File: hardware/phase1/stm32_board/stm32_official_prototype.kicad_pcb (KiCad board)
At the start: 6 copper layers, 75 parts, among them CN11 Conn_02x36_Odd_Even, CN12 Conn_02x36_Odd_Even, CN14 USB_B_Micro, CN5 Conn_ARM_JTAG_SWD_10, U1 STM32L496ZGTx, U12 STMPS2151STR, U4 ST890CDR, U5 USBLC6-2SC6, U6 LD39050PU33R, U8 TSV631AILT

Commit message: stm32 board update (1.11.25)
- correcting footprints (IP)
- left off on USB circuitry
- note: net labels must be corrected for differential pair
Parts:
- removed C11, C20, C26: 100nF, Capacitor,100nF,10%,16V,X7R,0603,YAGEO:CC0603N_YAG
- removed C16, C42: 4.7uF, TAN Capacitor,4.7uF,10%,16V,A Type,AVX:TAJA_AVX
- removed C17: 10uF, TAN Capacitor,10uF,10%,16V,A Type,AVX:CAPMP3216X180N
- removed C18: 10uF(25V), Tan Capacitor,10uF,10%,25V,Tan-B,TAJB106K025RNJ:CAPMP3516X190N
- removed C19, C27: 1uF_X5R_0603, Capacitor,1uF,0603,16V,10%,X5R,YAGEO:CAPC1608X90
- removed C45: 100nF, HDR_1x2_2R54:61300211121
- removed JP5: Conn_02x01, HDR_1x2_2R54:61300211121
- removed JP6: Conn_02x04_Odd_Even, 2x4_2R54:61300821121
- removed LD5, LD7: Red, LED-SMD-RED-DIFFUSED_0603_:LED-0603
- removed LD6, LD8: Green, SMD-LED-CLEAR-GREEN_0603_:LED-0603
- removed R22, R28: 1K, RC0603FR-071KL:RESC1607X60N
- removed R26, R52: 10K, RC0603FR-0710KL:RESC1607X60N
- removed R27: 2K7, RES_2.7K_0603_:R0603
- removed R41: 330, RC0603FR-07330RL:RESC1607X60N
- removed R45: 620, RC0603FR-07620RL:RESC1608X55N
- removed R48: 22K, RC0603FR-0722KL:RESC1607X60N
- removed R49, R51: 47K, RC0603FR-0747KL:RESC1608X55
- removed U12: STMPS2151STR, STMPS2151STR:SOT23-5L_STM
- removed U4: ST890CDR, ST890CDR:SO-8_STM
- removed U6: LD39050PU33R, LD39050PU33R:DFN6_3X3_STM
- added C40: [N/A], RC0603FR-07100RL:RESC1607X60N, F.Cu at (114.8, 117.8)
- added R46: 430K, RC0603FR-071K5L:RESC1607X60N, F.Cu at (90.8, 104.0)
- added R47: 620K, RC0603FR-071K5L:RESC1607X60N, F.Cu at (90.8, 106.5)
- added SB110: Open, RC0603JR-070RL:RESC1607X60N, F.Cu at (205.0, 46.6)
- added SB111: Open, RC0603JR-070RL:RESC1607X60N, F.Cu at (205.0, 49.1)
- added SB112: Closed, RC0603JR-070RL:RESC1607X60N, F.Cu at (205.0, 51.7)
- added SB123: Open, RC0603JR-070RL:RESC1607X60N, F.Cu at (205.0, 54.3)
- added SB124: Closed, RC0603JR-070RL:RESC1607X60N, F.Cu at (205.0, 56.8)
- added SB130: Closed, RC0603JR-070RL:RESC1607X60N, B.Cu at (147.4, 71.9)
- added SB131: Closed, RC0603JR-070RL:RESC1607X60N, B.Cu at (145.1, 71.9)
- added SB132: Closed, RC0603JR-070RL:RESC1607X60N, F.Cu at (209.0, 46.6)
- added SB142: Closed, RC0603JR-070RL:RESC1607X60N, B.Cu at (138.2, 81.8)
- added SB143: Closed, RC0603JR-070RL:RESC1607X60N, B.Cu at (136.0, 81.8)
- added SB149: Closed, RC0603JR-070RL:RESC1607X60N, F.Cu at (213.1, 41.4)
- added SB152: Closed, RC0603JR-070RL:RESC1607X60N, F.Cu at (213.1, 44.0)
- added SB154: Closed, RC0603JR-070RL:RESC1607X60N, B.Cu at (139.7, 99.5)
- added SB158: Closed, RC0603JR-070RL:RESC1607X60N, F.Cu at (213.1, 49.1)
- added SB162: RC0603JR-070RL, RC0603JR-070RL:RESC1607X60N, F.Cu at (213.1, 51.7)
- added SB166: Closed, RC0603JR-070RL:RESC1607X60N, F.Cu at (213.1, 54.3)
- added SB167: Open, RC0603JR-070RL:RESC1607X60N, F.Cu at (213.1, 56.8)
- added SB171: Circuit Breaker-SMPS, RC0603JR-070RL:RESC1607X60N, F.Cu at (217.2, 41.4)
- added SB172: RC0603JR-070RL, RC0603JR-070RL:RESC1607X60N, F.Cu at (217.2, 44.0)
- added SB197: Closed, RC0603JR-070RL:RESC1607X60N, F.Cu at (77.2, 68.8)
- added SB199: RC0603JR-070RL, RC0603JR-070RL:RESC1607X60N, F.Cu at (217.2, 49.1)
- added SB201: RC0603JR-070RL, RC0603JR-070RL:RESC1607X60N, F.Cu at (217.2, 51.7)
- added SWD: Conn_ARM_JTAG_SWD_10, SSW_105_06_G_D:SAMTEC_SSW-105-06-G-D, F.Cu at (136.1, 58.0)
- added U13: USBLC6-2SC6, Package_TO_SOT_SMD:SOT-23-6, F.Cu at (2.08, 8.40)
- added U9: ESDALC6V1W5, ESDALC6V1W5 (1):SOT323-5L, F.Cu at (135.6, 50.7)
- C49, C50, C51, C52, C53, C54, C60, C61, R54: moved to B.Cu
- L3: renamed from FB1; value FerriteBead_Small -> BEAD
- R46: footprint RC0603FR-07430KL:RESC1608X55N -> RC0603FR-071K5L:RESC1607X60N
- R47: footprint RC0603FR-07620KL:RESC1608X55N -> RC0603FR-071K5L:RESC1607X60N
- moved CN5 244.5 mm to (12.0, 4.02)
- moved R42 134.6 mm to (110.1, 117.8), turned to -90 degrees
- moved R43 131.6 mm to (112.5, 117.8), turned to -90 degrees
- moved R44 126.5 mm to (117.2, 117.8), turned to 90 degrees
- moved R54 116.1 mm to (129.6, 79.7), turned to -90 degrees
- moved R46 101.6 mm to (156.3, 116.1), turned to 90 degrees
- moved C49 100.3 mm to (130.7, 72.8), turned to 90 degrees
- moved C50 98.8 mm to (132.7, 72.8), turned to 90 degrees
- moved R47 98.6 mm to (158.5, 116.1), turned to 90 degrees
- moved U5 96.3 mm to (152.5, 121.5), turned to 90 degrees
- moved R50 95.7 mm to (156.6, 120.9), turned to 90 degrees
- moved C51 92.4 mm to (140.1, 72.2), turned to 90 degrees
- moved C61 91.2 mm to (142.7, 102.1), turned to -90 degrees
- moved D2 83.4 mm to (136.2, 66.9), turned to -90 degrees
- moved C53 81.1 mm to (152.6, 72.2), turned to 90 degrees
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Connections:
- C28 pad 1: IOREF -> VDD_MCU
- C29 pad 1: IOREF -> VDD_MCU
- C30 pad 1: IOREF -> VDD_MCU
- C31 pad 1: IOREF -> VDD
- C32 pad 1: IOREF -> VDD_MCU
- C33 pad 1: IOREF -> VDD_MCU
- C34 pad 1: IOREF -> VDD_MCU
- C49 pad 1: IOREF -> VDD_MCU
- C50 pad 1: IOREF -> VDD
- C51 pad 1: IOREF -> VDD
- C52 pad 1: IOREF -> VDD
- C53 pad 1: IOREF -> VDD_MCU
- C54 pad 1: IOREF -> VDD_MCU
- C56 pad 1: AVDD -> VREF+
- C57 pad 1: AVDD -> VREF+
- C60 pad 1: IOREF -> VBAT
- C61 pad 1: IOREF -> VDD_MCU
- CN11 pad 16: +3V3_PER -> +3V3
- CN11 pad 33: IOREF -> VBAT
- CN14 pad 1: PA9 -> USB_VBUS
- CN14 pad 4: PA10 -> unconnected-(CN14-ID-Pad4)
- D2 pad 1: IOREF -> VDD
- L3 pad 1: IOREF -> Net-(L3-Pad1)
- L3 pad 2: AVDD -> Net-(L3-Pad2)
- R29 pad 1: PB14 -> Net-(R29-Pad1)
- R30 pad 1: PB7 -> Net-(R30-Pad1)
- R37 pad 1: PC7 -> Net-(R37-Pad1)
- R38 pad 1: PH3-BOOT0 -> Net-(R38-Pad1)
- R43 pad 1: PC13 -> Net-(R43-Pad1)
- R44 pad 1: Net-(B1-Pad2) -> VDD_MCU
- R46 pad 1: VBUS_DET -> PA12
- R46 pad 2: PA9 -> Net-(R46-Pad2)
- R47 pad 2: VBUS_DET -> Net-(R46-Pad2)
- R50 pad 2: PG6 -> Net-(R50-Pad2)
- R54 pad 2: PA9 -> USB_VBUS
- U1 pad 106: IOREF -> VDD
- U1 pad 108: IOREF -> VDD_MCU
- U1 pad 121: IOREF -> VDD_MCU
- U1 pad 131: IOREF -> VDD
- U1 pad 144: IOREF -> VDD_MCU
- U1 pad 17: IOREF -> VDD_MCU
- U1 pad 32: AVDD -> VREF+
- U1 pad 39: IOREF -> VDD_MCU
- U1 pad 52: IOREF -> VDD_MCU
- U1 pad 6: IOREF -> VBAT
- U1 pad 62: IOREF -> VDD_MCU
- U1 pad 72: IOREF -> VDD_MCU
- U1 pad 84: IOREF -> VDD_MCU
- U1 pad 95: IOREF -> VDD
- U5 pad 5: PA9 -> USB_VBUS
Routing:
- net VDD_MCU: track 0.00 -> 20.7 mm, vias 0 -> 1
- net +5V: track 19.4 -> 0.00 mm
- net IOREF: track 19.1 -> 0.00 mm, vias 3 -> 0
- net VDD: track 0.00 -> 15.9 mm, vias 0 -> 2
- net PB3: track 0.00 -> 14.3 mm
- net PA12: track 0.00 -> 13.8 mm
- net NRST: track 0.00 -> 10.5 mm
- net VREF-: track 22.2 -> 15.1 mm, vias 3 -> 2
- net PA14: track 0.00 -> 6.81 mm
- net PA11: track 0.00 -> 5.40 mm
- net +3V3_PER: track 4.75 -> 0.00 mm, vias 1 -> 0
- net Net-(B1-Pad1): track 0.00 -> 4.71 mm
- net AVDD: track 7.27 -> 2.69 mm
- net VBAT: track 0.00 -> 3.00 mm, vias 0 -> 1
- net PA13: track 0.00 -> 2.53 mm
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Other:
- board text added: "1"
- board text added: "10"
- board text added: "2"
- board text added: "3"
- board text added: "4"
- board text added: "5"
- board text added: "6"
- board text added: "7"
- board text added: "8"
- board text added: "9"

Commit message: stm32 PCB board ~50% finished
- left off on verifying button footprint
(im trying to follow the original manufacturer BOM as much as possible, but some parts aren't downloadable.

- best solution is to use the notes column in the BOM, describes what the footprint is (SMT, 6x6mm, tactile switch, etc.)
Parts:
- added B1: TS02-66-60-BK-160-LCR-D, TS04_66_43_BK_260_SMT:SW_TS04-66-43-BK-260-SMT, F.Cu at (112.8, 124.4)
- added B2: TS02-66-60-BK-160-LCR-D, TS04_66_43_BK_260_SMT:SW_TS04-66-43-BK-260-SMT, F.Cu at (68.9, 137.8)
- added SB135: RC0603JR-070RL, RC0603JR-070RL:RESC1607X60N, B.Cu at (125.7, 79.5)
- C40: value [N/A] -> C_0603_1608Metric; footprint RC0603FR-07100RL:RESC1607X60N -> Capacitor_SMD:C_0603_1608Metric
- SB149, SB152, SB158, SB167, SB199, SB201: moved to B.Cu
- moved U13 172.4 mm to (128.0, 126.1)
- moved LD3 108.5 mm to (146.6, 51.5), turned to 90 degrees
- moved JP4 106.3 mm to (144.4, 61.1), turned to 180 degrees
- moved LD2 104.0 mm to (150.5, 51.5), turned to 90 degrees
- moved CN5 101.1 mm to (103.4, 47.2)
- moved LD1 99.7 mm to (154.3, 51.5), turned to 90 degrees
- moved R30 99.3 mm to (150.5, 55.3), turned to 180 degrees
- moved R29 96.9 mm to (146.6, 55.4), turned to 90 degrees
- moved R31 91.5 mm to (154.3, 55.3), turned to 90 degrees
- moved SB199 90.2 mm to (162.6, 120.9), turned to 90 degrees
- moved SB158 85.9 mm to (154.9, 112.3), turned to 90 degrees
- moved SB201 85.8 mm to (166.5, 120.9), turned to -90 degrees
- moved SB149 85.3 mm to (150.8, 99.6)
- moved SB152 81.6 mm to (157.5, 103.7), turned to 90 degrees
- moved SB167 78.5 mm to (157.5, 112.3), turned to 90 degrees
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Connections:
- C40 pad 1: VDD_MCU -> NetC40_1
- R38 pad 1: Net-(R38-Pad1) -> PH3-BOOT0
- R54 pad 1: PA9 -> Net-(R54-Pad1)
- SB171 pad 1: PH3-BOOT0 -> PH3
- SB171 pad 2: Net-(R38-Pad1) -> PH3-BOOT0
- SWD pad 03: VREF- -> GND
- SWD pad 05: VREF- -> GND
- SWD pad 09: VREF- -> GND
- U1 pad 138: PH3-BOOT0 -> PH3
- U13 pad 2: VREF- -> GND
- U9 pad GND: VREF- -> GND
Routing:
- net USB_VBUS: track 2.03 -> 68.0 mm, vias 1 -> 2
- net VREF-: track 15.1 -> 40.5 mm, vias 2 -> 32
- net Net-(B1-Pad1): track 4.71 -> 24.5 mm
- net GND: track 0.00 -> 18.6 mm, vias 0 -> 4
- net VDD: track 15.9 -> 27.9 mm, vias 2 -> 5
- net Net-(U8-IN-): track 2.73 -> 13.1 mm
- net VDD_MCU: track 20.7 -> 30.3 mm, vias 1 -> 8
- net VREF+: track 0.00 -> 6.85 mm, vias 0 -> 1
- net AVDD: track 2.69 -> 8.17 mm
- net Net-(L3-Pad1): track 0.00 -> 5.28 mm
- net Net-(L3-Pad2): track 0.00 -> 2.88 mm
- net NetC40_1: track 0.00 -> 2.46 mm
- net Net-(R54-Pad1): track 0.00 -> 2.20 mm
- net Net-(R46-Pad2): track 2.20 -> 3.73 mm, vias 1 -> 2
- net Net-(R50-Pad2): track 0.00 -> 1.44 mm, vias 1 -> 2
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
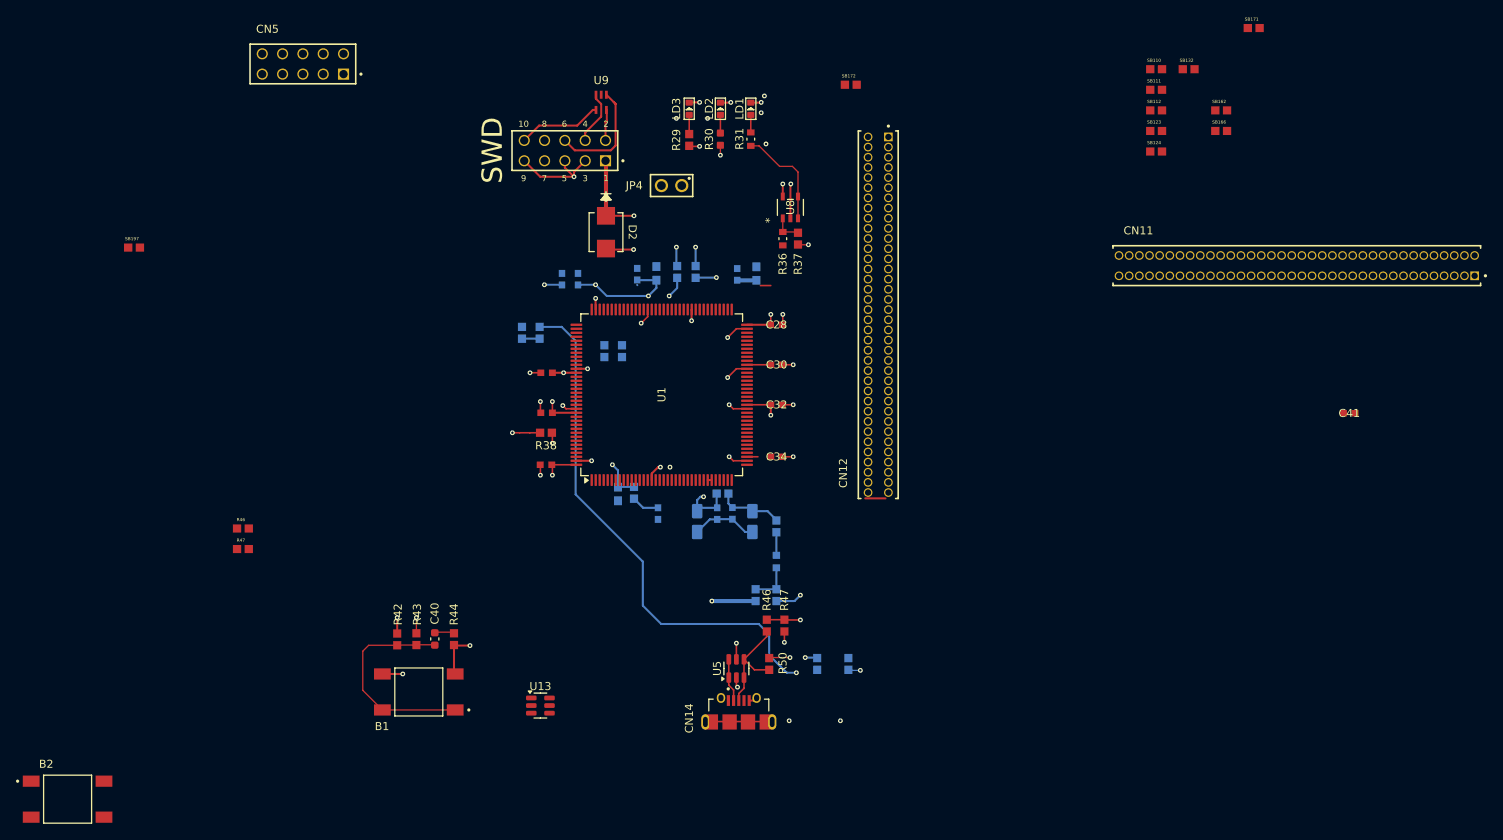
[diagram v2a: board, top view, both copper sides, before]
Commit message: stm32 pcb update for (1.13.25)
- most components are now connected
- need to verify a few more footprints
- board is ~65% finished
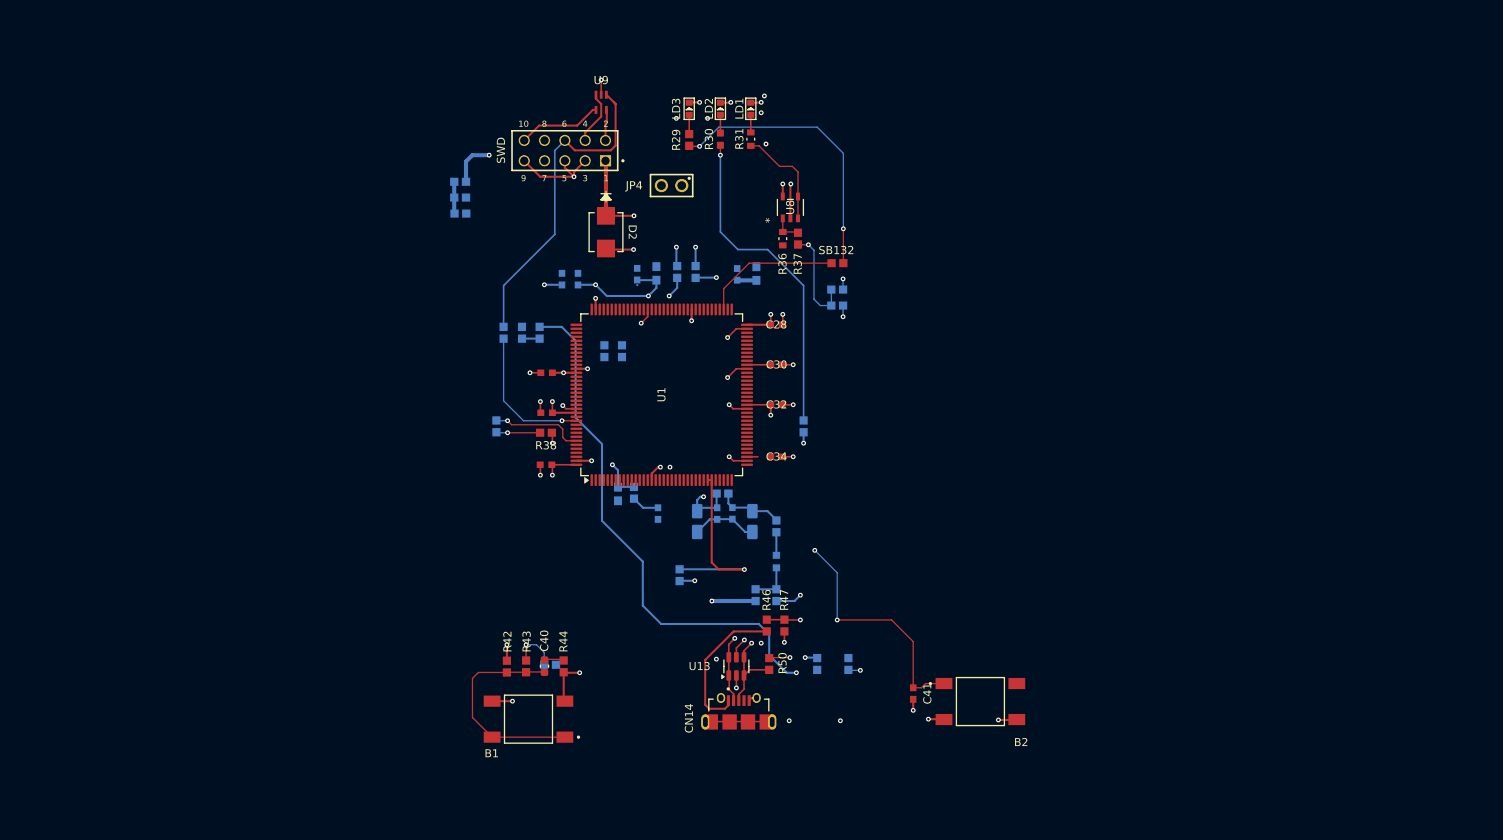
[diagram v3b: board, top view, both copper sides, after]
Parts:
- removed CN11, CN12: Conn_02x36_Odd_Even, SLM-136-01-S-D:SAMTEC_SLM-136-01-S-D
- removed CN5: Conn_ARM_JTAG_SWD_10, SSW_105_06_G_D:SAMTEC_SSW-105-06-G-D
- removed the R46 at (90.8, 104.0)
- removed the R47 at (90.8, 106.5)
- removed U5: USBLC6-2SC6, Package_TO_SOT_SMD:SOT-23-6
- B2: value TS02-66-60-BK-160-LCR-D -> RESET
- SB110, SB111, SB112, SB123, SB124, SB162, SB166, SB171, SB172, SB197: moved to B.Cu
- moved B2 114.8 mm to (183.0, 125.6)
- moved SB171 107.0 mm to (122.5, 91.2), turned to -90 degrees
- moved SB162 93.9 mm to (123.4, 79.5), turned to 90 degrees
- moved SB111 88.3 mm to (118.0, 64.6), turned to 180 degrees
- moved SB110 88.1 mm to (118.0, 60.6), turned to 180 degrees
- moved SB112 87.7 mm to (118.0, 62.6), turned to 180 degrees
- moved SB166 87.6 mm to (145.4, 109.8), turned to 90 degrees
- moved SB197 73.7 mm to (129.2, 121.0), turned to 180 degrees
- moved C41 64.8 mm to (174.6, 124.6), turned to 90 degrees
- moved SB132 50.1 mm to (165.1, 70.8)
- moved SB123 45.5 mm to (165.1, 76.1), turned to 180 degrees
- moved SB124 43.4 mm to (165.1, 74.1), turned to 180 degrees
- moved SB172 43.1 mm to (160.9, 91.2), turned to 90 degrees
- moved U13 25.0 mm to (152.5, 121.2), turned to 90 degrees
- moved R43 14.1 mm to (126.2, 121.2)
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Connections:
- B2 pad 1: VREF- -> GND
- B2 pad 4: VREF- -> GND
- C28 pad 2: VREF- -> GND
- C29 pad 2: VREF- -> GND
- C30 pad 2: VREF- -> GND
- C31 pad 2: VREF- -> GND
- C32 pad 2: VREF- -> GND
- C33 pad 2: VREF- -> GND
- C34 pad 2: VREF- -> GND
- C41 pad 2: VREF- -> GND
- C49 pad 2: VREF- -> GND
- C50 pad 2: VREF- -> GND
- C51 pad 2: VREF- -> GND
- C52 pad 2: VREF- -> GND
- C53 pad 2: VREF- -> GND
- C54 pad 2: VREF- -> GND
- C56 pad 2: VREF- -> GND
- C57 pad 2: VREF- -> GND
- C58 pad 2: VREF- -> GND
- C59 pad 2: VREF- -> GND
- C60 pad 2: VREF- -> GND
- C61 pad 2: VREF- -> GND
- CN14 pad 10: (no net) -> GND
- CN14 pad 5: VREF- -> GND
- CN14 pad 6: VREF- -> GND
- CN14 pad 7: (no net) -> GND
- CN14 pad 8: (no net) -> GND
- CN14 pad 9: (no net) -> GND
- D2 pad 2: VREF- -> GND
- LD1 pad -: (no net) -> GND
- LD2 pad -: (no net) -> GND
- LD3 pad -: (no net) -> GND
- R36 pad 1: VREF- -> GND
- R38 pad 2: VREF- -> GND
- R42 pad 1: VREF- -> GND
- R46 pad 1: PA12 -> USB_VBUS
- R47 pad 1: VREF- -> GND
- SB166 pad 1: VREF- -> GND
- SB166 pad 2: VREF- -> GND
- U1 pad 107: VREF- -> GND
- U1 pad 120: VREF- -> GND
- U1 pad 130: VREF- -> GND
- U1 pad 143: VREF- -> GND
- U1 pad 16: VREF- -> GND
- U1 pad 30: VREF- -> GND
- U1 pad 31: VREF- -> GND
- U1 pad 38: VREF- -> GND
- U1 pad 51: VREF- -> GND
- U1 pad 61: VREF- -> GND
- U1 pad 71: VREF- -> GND
- U1 pad 83: VREF- -> GND
- U1 pad 94: VREF- -> GND
- U8 pad 2: VREF- -> GND
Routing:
- net GND: track 18.6 -> 89.4 mm, vias 4 -> 44
- net PB3: track 14.3 -> 58.7 mm, vias 0 -> 1
- net VREF-: track 40.5 -> 0.00 mm, vias 32 -> 0
- net Net-(R30-Pad1): track 0.00 -> 39.6 mm
- net Net-(R29-Pad1): track 0.00 -> 34.0 mm, vias 1 -> 2
- net NRST: track 10.5 -> 41.6 mm, vias 0 -> 2
- net USB_VBUS: track 68.0 -> 87.5 mm
- net PB14: track 0.00 -> 17.4 mm
- net Net-(R37-Pad1): track 0.00 -> 11.6 mm
- net PH3: track 0.00 -> 10.3 mm, vias 0 -> 1
- net +3V3_PER: track 0.00 -> 5.76 mm, vias 1 -> 2
- net Net-(R43-Pad1): track 0.00 -> 4.20 mm
- net PH3-BOOT0: track 0.00 -> 4.06 mm
- net IOREF: track 0.00 -> 3.99 mm
- net PA12: track 13.8 -> 10.9 mm, vias 0 -> 1
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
